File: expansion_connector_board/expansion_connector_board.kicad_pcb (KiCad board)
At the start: 2 copper layers, 154 x 89 mm, 17 parts, among them J1 Conn_01x04, J12 Conn_02x17_Top_Bottom, J13 Conn_01x04, J14 Conn_02x17_Top_Bottom, J19 MEGA65 R4+ Analog Audio Header, J2 ESP32 JTAG+UART (TE0790), J3 ESP32 UART Breakout, J4 ESP32 Bootstraps, J5 ESP32 Sensor, J6 ESP32/Peripheral UART Interfa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, J7 Conn_01x04, U1 ESP32-WROOM-32D

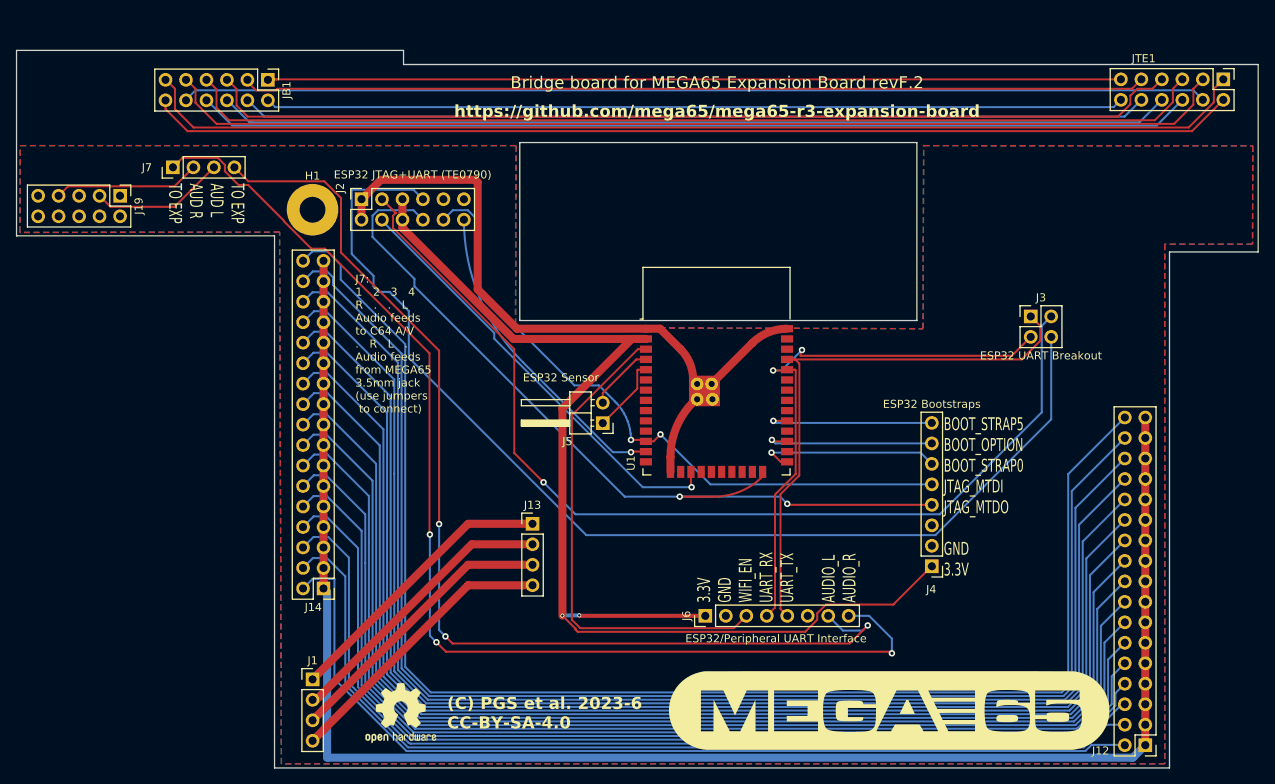
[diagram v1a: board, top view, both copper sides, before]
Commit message: rework bridge board for Pico Pi instead of ESP32
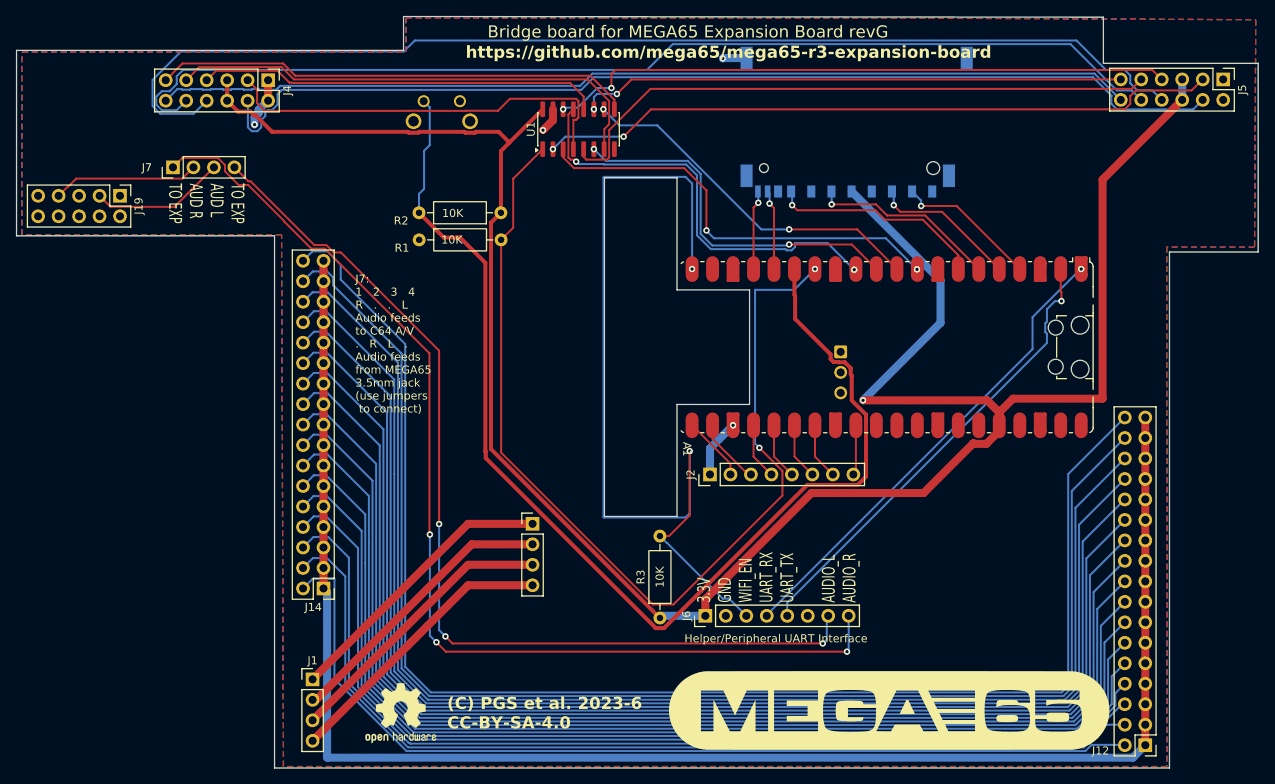
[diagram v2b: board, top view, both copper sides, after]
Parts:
- removed H1: TE0790 Orienting Hole for ESP32 JTAG, MountingHole:MountingHole_3.2mm_M3_Pad
- removed JB1, JTE1: Conn_02x06_Top_Bottom, Connector_PinHeader_2.54mm:PinHeader_2x06_P2.54mm_Vertical
- added A1: RaspberryPi_Pico_W, Module:RaspberryPi_Pico_W_SMD_HandSolder, F.Cu at (149.9, 71.8)
- added R1: 10K, Resistor_THT:R_Axial_DIN0207_L6.3mm_D2.5mm_P10.16mm_Horizontal, F.Cu at (102.1, 55.1)
- added R2: 10K, Resistor_THT:R_Axial_DIN0207_L6.3mm_D2.5mm_P10.16mm_Horizontal, F.Cu at (91.9, 58.5)
- added R3: 10K, Resistor_THT:R_Axial_DIN0207_L6.3mm_D2.5mm_P10.16mm_Horizontal, F.Cu at (121.8, 105.4)
- added SW1: WRITE REQUEST PUSH BUTTON, snapeda:TE_2-1825027-0, B.Cu at (94.8, 42.5)
- J1, J13: value Conn_01x04 -> POWER RELAY
- J2: value ESP32 JTAG+UART (TE0790) -> GPIO Breakout; footprint Connector_PinHeader_2.54mm:PinHeader_2x06_P2.54mm_Vertical -> Connector_PinHeader_2.54mm:PinHeader_1x08_P2.54mm_Vertical
- J3: value ESP32 UART Breakout -> 693063020911; footprint Connector_PinHeader_2.54mm:PinHeader_2x02_P2.54mm_Vertical -> snapeda:693063020911; moved to B.Cu
- J4: value ESP32 Bootstraps -> MEGA65 JTAG+SERIAL HEADER; footprint Connector_PinHeader_2.54mm:PinHeader_1x08_P2.54mm_Vertical -> Connector_PinHeader_2.54mm:PinHeader_2x06_P2.54mm_Vertical
- J5: value ESP32 Sensor -> EXP BOARD TE0790 RELAY; footprint Connector_PinHeader_2.54mm:PinHeader_1x02_P2.54mm_Horizontal -> Connector_PinHeader_2.54mm:PinHeader_2x06_P2.54mm_Vertical
- J6: value ESP32/Peripheral UART Interface -> Helper/Peripheral UART Interface
- U1: value ESP32-WROOM-32D -> 74CBTLV3257; footprint RF_Module:ESP32-WROOM-32D -> Package_SO:SOIC-16_3.9x9.9mm_P1.27mm
- moved J4 102.0 mm to (73.2, 38.7), turned to -90 degrees
- moved J5 88.0 mm to (191.7, 38.6), turned to -90 degrees
- moved J2 53.5 mm to (128.0, 87.6)
- moved U1 37.2 mm to (111.7, 44.8), turned to 90 degrees
- moved J3 32.8 mm to (146.2, 43.3)
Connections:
- J2 pad 2: GND -> Net-(A1-GPIO16)
- J2 pad 3: /TE0790_A -> Net-(A1-GPIO17)
- J2 pad 4: JTAG_MTCK -> Net-(A1-GPIO18)
- J2 pad 5: +3.3V -> Net-(A1-GPIO19)
- J2 pad 6: +3.3V -> Net-(A1-GPIO20)
- J2 pad 7: /TE0790_B -> Net-(A1-GPIO21)
- J2 pad 8: JTAG_MTDO -> Net-(A1-GPIO22)
- J3 pad 1: UART_TX -> SD_CS
- J3 pad 2: /TE0790_A -> SD_MOSI
- J3 pad 3: UART_RX -> GND
- J3 pad 4: /TE0790_B -> +3.3V
- J4 pad 1: +3.3V -> GND
- J4 pad 3: unconnected-(J4-Pin_3-Pad3) -> MEGA65_TCK
- J4 pad 4: JTAG_MTDO -> Net-(J4-Pin_4)
- J4 pad 5: JTAG_MTDI -> +3.3V
- J4 pad 6: BOOT_STRAP0 -> +3.3V
- J4 pad 7: BOOT_OPTION -> MEGA65_TDO
- J4 pad 8: BOOT_STRAP5 -> Net-(J4-Pin_8)
- J5 pad 1: Net-(J5-Pin_1) -> GND
- J5 pad 2: Net-(J5-Pin_2) -> GND
- J6 pad 4: UART_RX -> MEGA65_UART_RX
- J6 pad 5: UART_TX -> MEGA65_UART_TX
- U1 pad 1: GND -> JTAG_HIJACK
- U1 pad 10: unconnected-(U1-IO25-Pad10) -> PICO_TMS
- U1 pad 11: unconnected-(U1-IO26-Pad11) -> TE0790_TMS
- U1 pad 12: JTAG_MTDI -> MEGA65_TDO
- U1 pad 13: JTAG_MTMS -> PICO_TDO
- U1 pad 14: unconnected-(U1-IO12-Pad14) -> TE0790_TDO
- U1 pad 16: unconnected-(U1-IO13-Pad16) -> +3.3V
- U1 pad 2: +3.3V -> TE0790_TCK
- U1 pad 3: WIFI_EN -> PICO_TCK
- U1 pad 4: Net-(J5-Pin_2) -> MEGA65_TCK
- U1 pad 5: Net-(J5-Pin_1) -> TE0790_TDI
- U1 pad 6: unconnected-(U1-IO34-Pad6) -> PICO_TDI
- U1 pad 7: unconnected-(U1-IO35-Pad7) -> MEGA65_TDI
- U1 pad 8: unconnected-(U1-IO32-Pad8) -> GND
- U1 pad 9: unconnected-(U1-IO33-Pad9) -> MEGA65_TMS
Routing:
- net SD_WRITE_GRANT: track 0.00 -> 143.6 mm
- net Net-(J4-Pin_8): track 0.00 -> 141.8 mm
- net /TE0790_B: track 138.8 -> 0.00 mm
- net Net-(JB1-Pin_11): track 138.6 -> 0.00 mm
- net Net-(JB1-Pin_12): track 135.1 -> 0.00 mm
- net Net-(J4-Pin_10): track 0.00 -> 133.8 mm
- net Net-(JB1-Pin_9): track 132.9 -> 0.00 mm
- net +3.3V: track 147.8 -> 278.8 mm, vias 2 -> 1
- net Net-(J4-Pin_4): track 0.00 -> 129.0 mm
- net Net-(JB1-Pin_7): track 127.6 -> 0.00 mm
- net Net-(JB1-Pin_10): track 127.1 -> 0.00 mm
- net /TE0790_A: track 124.8 -> 0.00 mm, vias 1 -> 0
- net Net-(JB1-Pin_8): track 123.7 -> 0.00 mm
- net JTAG_HIJACK: track 0.00 -> 123.5 mm, vias 0 -> 2
- net Net-(J4-Pin_12): track 0.00 -> 121.6 mm
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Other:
- board size 154 x 89 mm -> 154 x 93.2 mm
- board text added: "Bridge board for MEGA65 Expansion Board revG"
- board text added: "^ Suggested board edge for RF ^"
- board text removed: "BOOT_STRAP5 BOOT_OPTION BOOT_STRAP0 JTAG_MTDI JTAG_MTDO GND 3.3V"
- board text removed: "Bridge board for MEGA65 Expansion Board revF.2"
- board text removed: "ESP32 Sensor"

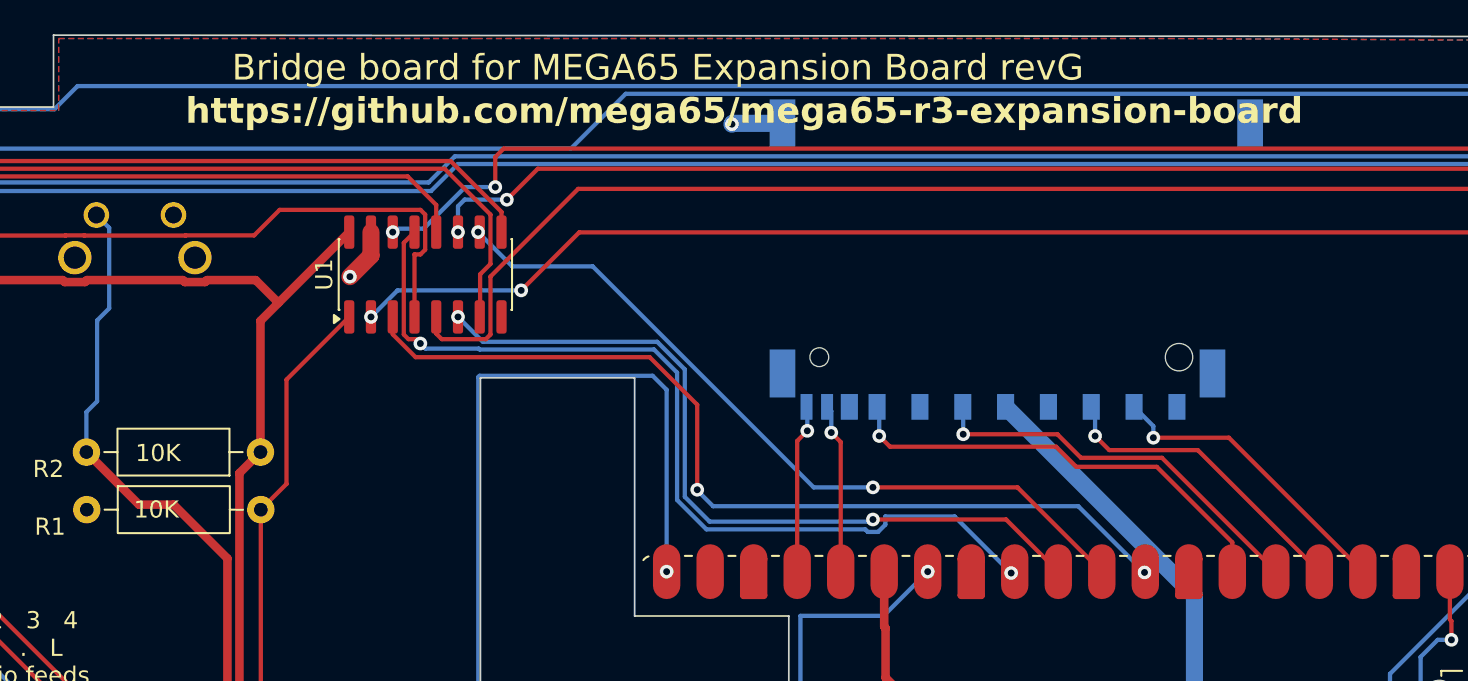
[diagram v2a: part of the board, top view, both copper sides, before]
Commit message: use hardware SPI pinout
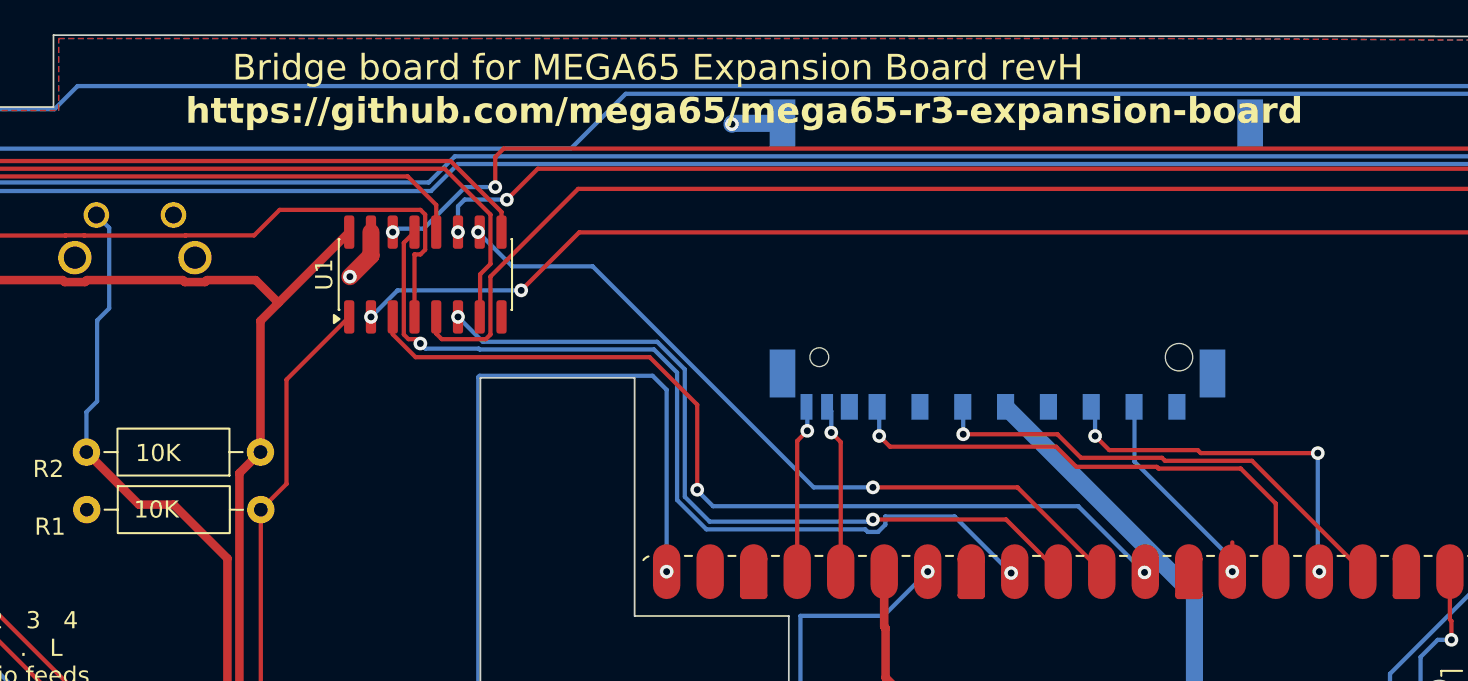
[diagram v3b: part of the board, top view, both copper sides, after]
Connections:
- A1 pad 4: SD_CS -> SD_CLK
- A1 pad 6: SD_CLK -> SD_MISO
- A1 pad 7: SD_MISO -> SD_CS
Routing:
- net SD_CLK: track 23.2 -> 28.3 mm
- net SD_MOSI: track 18.2 -> 22.2 mm, vias 1 -> 3
- net SD_MISO: track 26.6 -> 30.5 mm
- net SD_CS: track 17.7 -> 14.0 mm
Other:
- board text added: "Bridge board for MEGA65 Expansion Board revH"
- board text removed: "Bridge board for MEGA65 Expansion Board revG"
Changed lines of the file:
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@@
 			(layers "F.Cu" "F.Mask")
 			(roundrect_rratio 0.5)
-			(net 39 "SD_CS")
+			(net 45 "SD_CLK")
 			(pinfunction "GPIO2")
 			(pintype "bidirectional")
@@
 			(layers "F.Cu" "F.Mask")
 			(roundrect_rratio 0.5)
-			(net 45 "SD_CLK")
+			(net 24 "SD_MISO")
 			(pinfunction "GPIO4")
 			(pintype "bidirectional")
@@
 			(layers "F.Cu" "F.Mask")
 			(roundrect_rratio 0.5)
-			(net 24 "SD_MISO")
+			(net 39 "SD_CS")
 			(pinfunction "GPIO5")
 			(pintype "bidirectional")
@@
 		)
 	)
-	(gr_text "Bridge board for MEGA65 Expansion Board revG"
+	(gr_text "Bridge board for MEGA65 Expansion Board revH\n"
 		(at 125.275 32.7 0)
 		(layer "F.SilkS")
@@
 	)
 	(segment
-		(start 149.7 56)
-		(end 148.525 54.825)
+		(start 159.3 56.1)
+		(end 161.35 58.15)
 		(width 0.25)
 		(layer "F.Cu")
@@
 	)
 	(segment
-		(start 158.81 62.12)
-		(end 158.81 60.41)
+		(start 154.4 56)
+		(end 154.5 56.1)
 		(width 0.25)
 		(layer "F.Cu")
@@
 	)
 	(segment
-		(start 154.4 56)
-		(end 149.7 56)
+		(start 138.825 54.825)
+		(end 148.525 54.825)
 		(width 0.25)
 		(layer "F.Cu")
@@
 	)
 	(segment
-		(start 138.825 54.825)
-		(end 138.2 54.2)
+		(start 161.35 58.15)
+		(end 161.35 62.12)
+		(width 0.25)
+		(layer "F.Cu")
+		(net 24)
+	)
+	(segment
+		(start 138.2 54.2)
+		(end 138.825 54.825)
 		(width 0.25)
 		(layer "F.Cu")
@@
 	)
 	(segment
-		(start 158.81 60.41)
+		(start 149.7 56)
 		(end 154.4 56)
 		(width 0.25)
@@
 	)
 	(segment
+		(start 154.5 56.1)
+		(end 159.3 56.1)
+		(width 0.25)
+		(layer "F.Cu")
+		(net 24)
+	)
+	(segment
 		(start 148.525 54.825)
-		(end 138.825 54.825)
+		(end 149.7 56)
 		(width 0.25)
 		(layer "F.Cu")
@@
 	)
 	(segment
-		(start 158.61 54.3)
-		(end 154.2 54.3)
-		(width 0.25)
-		(layer "F.Cu")
-		(net 39)
-	)
-	(segment
-		(start 166.43 62.12)
-		(end 158.61 54.3)
+		(start 158.81 62.12)
+		(end 158.81 60.41)
 		(width 0.25)
 		(layer "F.Cu")
@@
 	)
 	(via
-		(at 154.2 54.3)
+		(at 158.81 62.12)
 		(size 0.8)
 		(drill 0.4)
@@
 	)
 	(segment
-		(start 154.2 53.625)
-		(end 153.075 52.5)
+		(start 153.1 55.7)
+		(end 158.81 61.41)
+		(width 0.25)
+		(layer "B.Cu")
+		(net 39)
+	)
+	(segment
+		(start 158.6 61.91)
+		(end 158.81 62.12)
+		(width 0.25)
+		(layer "B.Cu")
+		(net 39)
+	)
+	(segment
+		(start 153.1 52.525)
+		(end 153.1 55.7)
+		(width 0.25)
+		(layer "B.Cu")
+		(net 39)
+	)
+	(segment
+		(start 153.075 52.5)
+		(end 153.1 52.525)
 		(width 0.25)
 		(layer "B.Cu")
@@
 	)
 	(segment
-		(start 154.2 54.3)
-		(end 154.2 53.625)
+		(start 158.81 61.41)
+		(end 158.81 62.12)
 		(width 0.25)
 		(layer "B.Cu")
@@
 	)
 	(segment
-		(start 163.89 62.12)
-		(end 156.795 55.025)
+		(start 156.97 55.2)
+		(end 163.8 55.2)
 		(width 0.25)
 		(layer "F.Cu")
@@
 		(net 42)
 	)
+	(segment
+		(start 156.795 55.025)
+		(end 156.97 55.2)
+		(width 0.25)
+		(layer "F.Cu")
+		(net 42)
+	)
+	(via
+		(at 163.8 55.2)
+		(size 0.8)
+		(drill 0.4)
+		(layers "F.Cu" "B.Cu")
+		(net 42)
+	)
+	(via
+		(at 163.89 62.12)
+		(size 0.8)
+		(drill 0.4)
+		(layers "F.Cu" "B.Cu")
+		(net 42)
+	)
 	(via
 		(at 150.8 54.2)
@@
 	)
 	(segment
+		(start 163.8 62.03)
+		(end 163.89 62.12)
+		(width 0.25)
+		(layer "B.Cu")
+		(net 42)
+	)
+	(segment
 		(start 150.8 54.2)
 		(end 150.8 52.725)
@@
 	)
 	(segment
+		(start 163.8 55.2)
+		(end 163.8 62.03)
+		(width 0.25)
+		(layer "B.Cu")
+		(net 42)
+	)
+	(segment
 		(start 150.8 52.725)
 		(end 150.575 52.5)
@@
 	)
 	(segment
-		(start 161.35 62.12)
-		(end 154.705 55.475)
+		(start 159.96 55.65)
+		(end 166.43 62.12)
+		(width 0.25)
+		(layer "F.Cu")
+		(net 45)
+	)
+	(segment
+		(start 154.705 55.475)
+		(end 154.88 55.65)
 		(width 0.25)
 		(layer "F.Cu")
@@
 		(width 0.25)
 		(layer "F.Cu")
+		(net 45)
+	)
+	(segment
+		(start 154.88 55.65)
+		(end 159.96 55.65)
+		(width 0.25)
+		(layer "F.Cu")

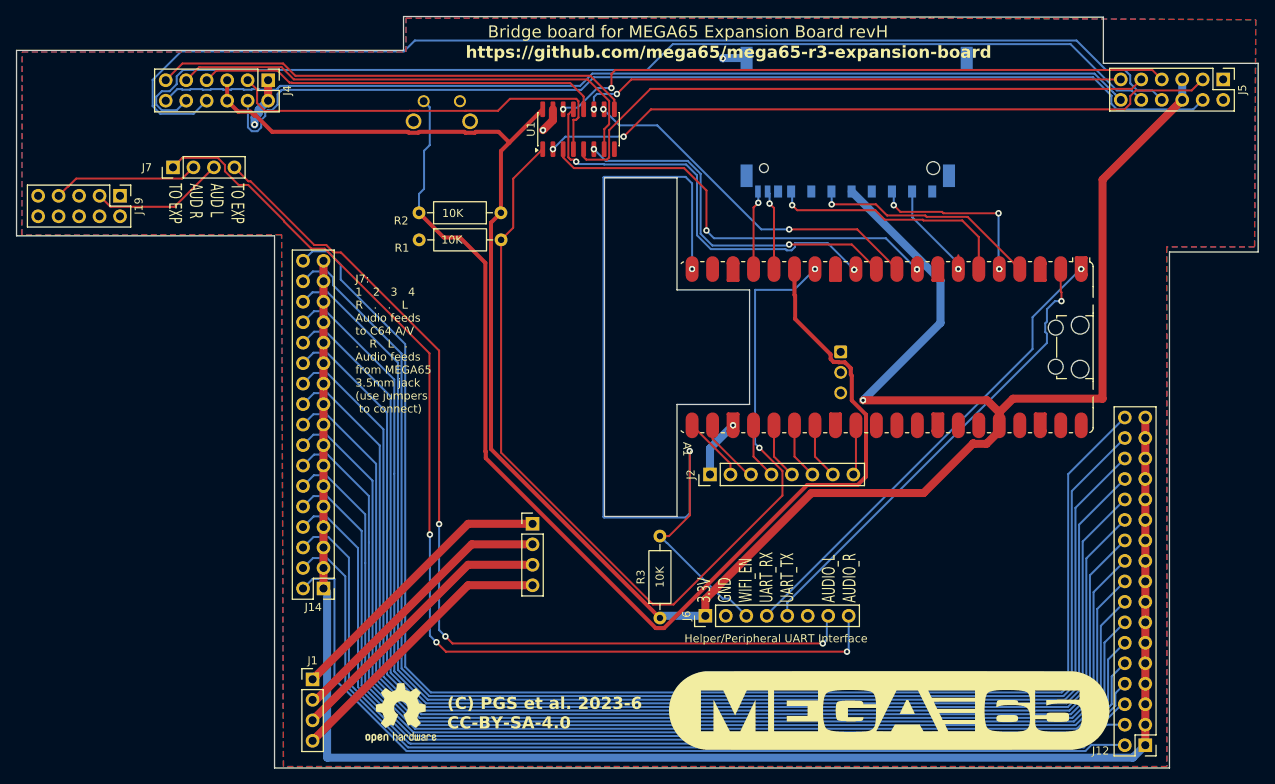
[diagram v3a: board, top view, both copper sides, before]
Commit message: protect 3.3v from MEGA65 into Pico Pi and generl tidying
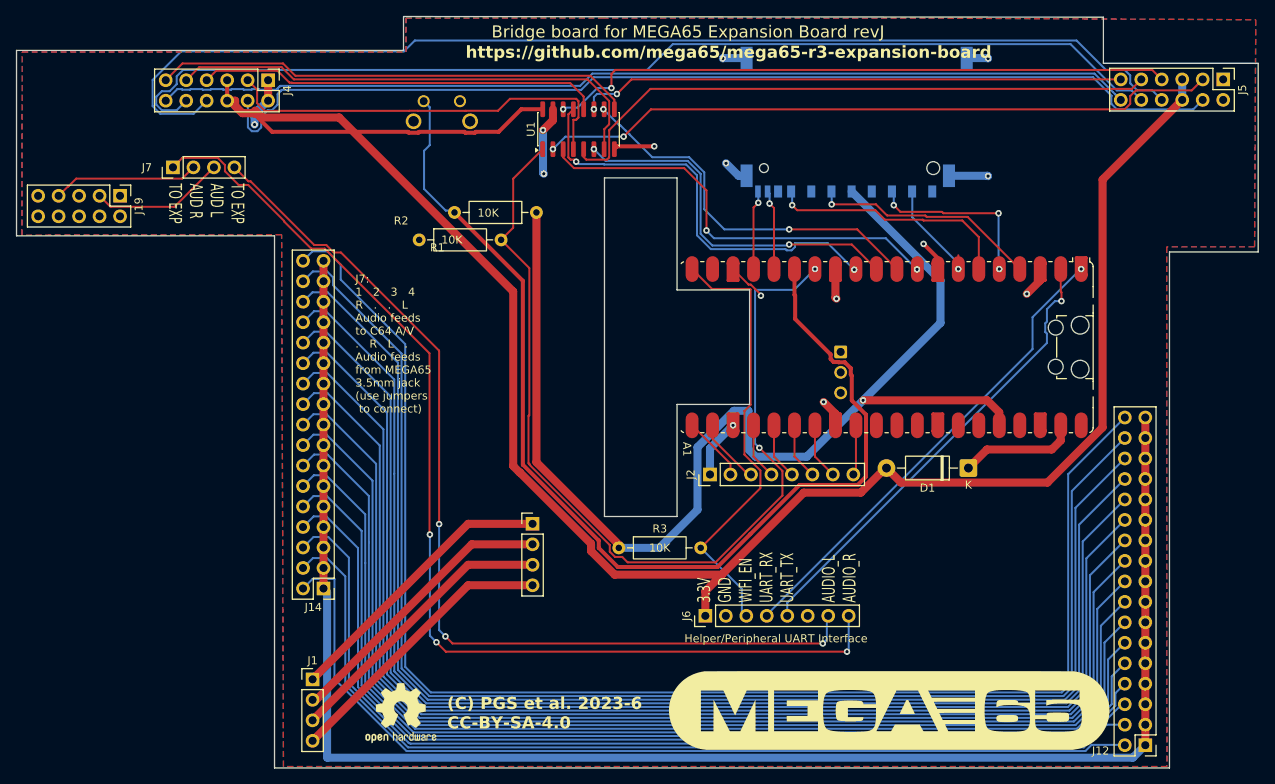
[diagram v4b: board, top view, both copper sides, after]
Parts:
- added D1: 1N5819, Diode_THT:D_DO-41_SOD81_P10.16mm_Horizontal, F.Cu at (160.1, 86.8)
- moved R3 10.1 mm to (116.7, 96.7), turned to 0 degrees
- moved R1 4.40 mm to (106.5, 55.1)
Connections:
- A1 pad 39: unconnected-(A1-VSYS-Pad39) -> Net-(A1-VSYS)
- J4 pad 5: +3.3V -> MEGA6_3V3
- J4 pad 6: +3.3V -> MEGA6_3V3
- J5 pad 5: +3.3V -> MEGA6_3V3
- J5 pad 6: +3.3V -> MEGA6_3V3
- J6 pad 1: +3.3V -> MEGA6_3V3
- U1 pad 16: +3.3V -> MEGA6_3V3
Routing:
- net MEGA6_3V3: track 0.00 -> 253.8 mm
- net +3.3V: track 278.8 -> 150.1 mm
- net WIFI_EN: track 110.3 -> 55.3 mm, vias 2 -> 0
- net GND: track 19.6 -> 61.7 mm, vias 4 -> 14
- net Net-(A1-VSYS): track 0.00 -> 14.8 mm
- net SD_WRITE_GRANT: track 143.6 -> 134.4 mm
- net JTAG_HIJACK: track 123.5 -> 118.5 mm
- net PICO_TMS: track 44.6 -> 47.3 mm
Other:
- board text added: "Bridge board for MEGA65 Expansion Board revJ"
- board text removed: "Bridge board for MEGA65 Expansion Board revH"
